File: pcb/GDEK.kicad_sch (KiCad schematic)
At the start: 266 parts, among them J1 TYPE-C-31-M-13C, J101 TYPE-C-31-M-13C, J102 AudioJack4, J103 Debug pads, J2 AudioJack4, J3 Debug pads, SW1 SK6812MINI, SW10 SK6812MINI, SW101 SK6812MINI, SW102 SK6812MINI, SW103 SK6812MINI, SW104 SK6812MINI, SW105 SK6812MINI, SW106 SK6812MINI, SW107 SK6812MINI, SW108 SK6812MINI, SW109 SK6812MINI, SW11 SK6812MINI, SW110 SK6812MINI, SW111 SK6812MINI, SW112 SK6812MINI, SW113 SK6812MINI, SW114 SK6812MINI, SW115 SK6812MINI, SW116 SK6812MINI, SW117 SK6812MINI, SW118 SK6812MINI, SW119 SK6812MINI, SW12 SK6812MINI, SW120 SK6812MINI, SW121 SK6812MINI, SW122 SK6812MINI, SW123 SK6812MINI, SW124 SK6812MINI, SW125 SK6812MINI, SW126 SK6812MINI, SW127 SK6812MINI, SW128 SK6812MINI, SW129 SK6812MINI, SW13 SK6812MINI, SW130 SK6812MINI, SW131 RotaryEncoder_Switch, SW14 SK6812MINI, SW15 SK6812MINI, SW16 SK6812MINI, SW17 SK6812MINI, SW18 SK6812MINI, SW19 SK6812MINI, SW2 SK6812MINI, SW20 SK6812MINI, SW21 SK6812MINI, SW22 SK6812MINI, SW23 SK6812MINI, SW24 SK6812MINI, SW25 SK6812MINI, SW26 SK6812MINI, SW27 SK6812MINI, SW28 SK6812MINI, SW29 SK6812MINI, SW3 SK6812MINI, SW30 SK6812MINI, SW31 RotaryEncoder_Switch, SW4 SK6812MINI, SW5 SK6812MINI, SW6 SK6812MINI, SW7 SK6812MINI, SW8 SK6812MINI, SW9 SK6812MINI, U1 RP2040, U101 RP2040, U102 W25Q128JVS, U103 74AHCT1G125, U104 USBLC6-2P6, U105 XC6210B332MR, U2 W25Q128JVS, U3 74AHCT1G125, U4 USBLC6-2P6, U5 XC6210B332MR, Y1 ABM8-272-T3, Y101 ABM8-272-T3

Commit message: ♻️ Replace LED and reroute them
They are flipped on odd rows to have a better layout not requiring any layer switch because of the new LED footprint with mouse ears.
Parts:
- removed SW1, SW10, SW101, SW102, SW103, SW104, SW105, SW106, SW107, SW108, SW109, SW11, SW110, SW111, SW112, SW113, SW114, SW115, SW116, SW117, SW118, SW119, SW12, SW120, SW121, SW122, SW123, SW124, SW125, SW126, SW127, SW128, SW129, SW13, SW130, SW14, SW15, SW16, SW17, SW18, SW19, SW2, SW20, SW21, SW22, SW23, SW24, SW25, SW26, SW27, SW28, SW29, SW3, SW30, SW4, SW5, SW6, SW7, SW8, SW9: SK6812MINI, GDEK:MX+KailhChoc+GateronKS+SK6812MINI-E_Tight, symbol GDEK:SW+SK6812MINIE
- added LD1, LD10, LD101, LD102, LD103, LD104, LD105, LD106, LD107, LD108, LD109, LD11, LD110, LD111, LD112, LD113, LD114, LD115, LD116, LD117, LD118, LD119, LD12, LD120, LD121, LD122, LD123, LD124, LD125, LD126, LD127, LD128, LD129, LD13, LD130, LD14, LD15, LD16, LD17, LD18, LD19, LD2, LD20, LD21, LD22, LD23, LD24, LD25, LD26, LD27, LD28, LD29, LD3, LD30, LD4, LD5, LD6, LD7, LD8, LD9: SK6812, GDEK:SK6812MINIE, symbol LED:SK6812
- added SW1, SW10, SW101, SW102, SW103, SW104, SW105, SW106, SW107, SW108, SW109, SW11, SW110, SW111, SW112, SW113, SW114, SW115, SW116, SW117, SW118, SW119, SW12, SW120, SW121, SW122, SW123, SW124, SW125, SW126, SW127, SW128, SW129, SW13, SW130, SW14, SW15, SW16, SW17, SW18, SW19, SW2, SW20, SW21, SW22, SW23, SW24, SW25, SW26, SW27, SW28, SW29, SW3, SW30, SW4, SW5, SW6, SW7, SW8, SW9: SW_Push_45deg, GDEK:MX+KailhChoc+GateronKS_Tight, symbol Switch:SW_Push_45deg
- U102, U2: footprint Package_SO:SOIC-8_5.23x5.23mm_P1.27mm -> Package_SO:SOIC-8_5.3x5.3mm_P1.27mm
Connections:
- net +5V: now also LD1.3 (VDD), LD10.3 (VDD), LD11.3 (VDD), LD12.3 (VDD), LD13.3 (VDD), LD14.3 (VDD), LD15.3 (VDD), LD16.3 (VDD), LD17.3 (VDD), LD18.3 (VDD), LD19.3 (VDD), LD2.3 (VDD), LD20.3 (VDD), LD21.3 (VDD), LD22.3 (VDD), LD23.3 (VDD), LD24.3 (VDD), LD25.3 (VDD), LD26.3 (VDD), LD27.3 (VDD), LD28.3 (VDD), LD29.3 (VDD), LD3.3 (VDD), LD30.3 (VDD), LD4.3 (VDD), LD5.3 (VDD), LD6.3 (VDD), LD7.3 (VDD), LD8.3 (VDD), LD9.3 (VDD)
- net +5V_R: now also LD101.3 (VDD), LD102.3 (VDD), LD103.3 (VDD), LD104.3 (VDD), LD105.3 (VDD), LD106.3 (VDD), LD107.3 (VDD), LD108.3 (VDD), LD109.3 (VDD), LD110.3 (VDD), LD111.3 (VDD), LD112.3 (VDD), LD113.3 (VDD), LD114.3 (VDD), LD115.3 (VDD), LD116.3 (VDD), LD117.3 (VDD), LD118.3 (VDD), LD119.3 (VDD), LD120.3 (VDD), LD121.3 (VDD), LD122.3 (VDD), LD123.3 (VDD), LD124.3 (VDD), LD125.3 (VDD), LD126.3 (VDD), LD127.3 (VDD), LD128.3 (VDD), LD129.3 (VDD), LD130.3 (VDD)
- net COL0: now also SW1.1, SW13.1, SW19.1, SW25.1, SW7.1
- net COL0_R: now also SW101.1, SW107.1, SW113.1, SW119.1, SW125.1
- net COL1: now also SW14.1, SW2.1, SW20.1, SW26.1, SW8.1
- net COL1_R: now also SW102.1, SW108.1, SW114.1, SW120.1, SW126.1
- net COL2: now also SW15.1, SW21.1, SW27.1, SW3.1, SW9.1
- net COL2_R: now also SW103.1, SW109.1, SW115.1, SW121.1, SW127.1
- net COL3: now also SW10.1, SW16.1, SW22.1, SW28.1, SW4.1
- net COL3_R: now also SW104.1, SW110.1, SW116.1, SW122.1, SW128.1
- net COL4: now also SW11.1, SW17.1, SW23.1, SW29.1, SW5.1
- net COL4_R: now also SW105.1, SW111.1, SW117.1, SW123.1, SW129.1
- net COL5: now also SW12.1, SW18.1, SW24.1, SW30.1, SW6.1
- net COL5_R: now also SW106.1, SW112.1, SW118.1, SW124.1, SW130.1
- net GND: now also LD1.1 (VSS), LD10.1 (VSS), LD11.1 (VSS), LD12.1 (VSS), LD13.1 (VSS), LD14.1 (VSS), LD15.1 (VSS), LD16.1 (VSS), LD17.1 (VSS), LD18.1 (VSS), LD19.1 (VSS), LD2.1 (VSS), LD20.1 (VSS), LD21.1 (VSS), LD22.1 (VSS), LD23.1 (VSS), LD24.1 (VSS), LD25.1 (VSS), LD26.1 (VSS), LD27.1 (VSS), LD28.1 (VSS), LD29.1 (VSS), LD3.1 (VSS), LD30.1 (VSS), LD4.1 (VSS), LD5.1 (VSS), LD6.1 (VSS), LD7.1 (VSS), LD8.1 (VSS), LD9.1 (VSS)
- net GND_R: now also LD101.1 (VSS), LD102.1 (VSS), LD103.1 (VSS), LD104.1 (VSS), LD105.1 (VSS), LD106.1 (VSS), LD107.1 (VSS), LD108.1 (VSS), LD109.1 (VSS), LD110.1 (VSS), LD111.1 (VSS), LD112.1 (VSS), LD113.1 (VSS), LD114.1 (VSS), LD115.1 (VSS), LD116.1 (VSS), LD117.1 (VSS), LD118.1 (VSS), LD119.1 (VSS), LD120.1 (VSS), LD121.1 (VSS), LD122.1 (VSS), LD123.1 (VSS), LD124.1 (VSS), LD125.1 (VSS), LD126.1 (VSS), LD127.1 (VSS), LD128.1 (VSS), LD129.1 (VSS), LD130.1 (VSS)
- net at D30.2 (A): now also SW30.2
- net at D120.2 (A): now also SW120.2
- net at D17.2 (A): now also SW17.2
- net at D110.2 (A): now also SW110.2
- net at D121.2 (A): now also SW121.2
- net at D29.2 (A): now also SW29.2
- net at D10.2 (A): now also SW10.2
- net at D128.2 (A): now also SW128.2
- net at D16.2 (A): now also SW16.2
- net at D126.2 (A): now also SW126.2
- net at U103.4: now also LD106.2 (DIN)
- net at D14.2 (A): now also SW14.2
- net at D23.2 (A): now also SW23.2
- net at D9.2 (A): now also SW9.2
- net at D25.2 (A): now also SW25.2
- net at D115.2 (A): now also SW115.2
- net at D4.2 (A): now also SW4.2
- net at D124.2 (A): now also SW124.2
- net at D20.2 (A): now also SW20.2
- net at D7.2 (A): now also SW7.2
- net at D22.2 (A): now also SW22.2
- net at D18.2 (A): now also SW18.2
- net at D101.2 (A): now also SW101.2
- net at D15.2 (A): now also SW15.2
- net at D2.2 (A): now also SW2.2
- net at D109.2 (A): now also SW109.2
- net at D127.2 (A): now also SW127.2
- net at D13.2 (A): now also SW13.2
- net at D26.2 (A): now also SW26.2
- net at D21.2 (A): now also SW21.2
- net at D106.2 (A): now also SW106.2
- net at D122.2 (A): now also SW122.2
- net at D3.2 (A): now also SW3.2
- net at D117.2 (A): now also SW117.2
- net at D130.2 (A): now also SW130.2
- net at D107.2 (A): now also SW107.2
- net at D119.2 (A): now also SW119.2
- net at D28.2 (A): now also SW28.2
- net at D8.2 (A): now also SW8.2
- net at D11.2 (A): now also SW11.2
- net at D5.2 (A): now also SW5.2
- net at D102.2 (A): now also SW102.2
- net at D24.2 (A): now also SW24.2
- net at D118.2 (A): now also SW118.2
- net at D104.2 (A): now also SW104.2
- net at D129.2 (A): now also SW129.2
- net at D12.2 (A): now also SW12.2
- net at D6.2 (A): now also SW6.2
- net at D108.2 (A): now also SW108.2
- net at D27.2 (A): now also SW27.2
- net at D103.2 (A): now also SW103.2
- net at D123.2 (A): now also SW123.2
- net at D1.2 (A): now also SW1.2
- net at U3.4: now also LD6.2 (DIN)
- net at D113.2 (A): now also SW113.2
- net at D114.2 (A): now also SW114.2
- net at D19.2 (A): now also SW19.2
- net at D105.2 (A): now also SW105.2
- net at D125.2 (A): now also SW125.2
- net at D111.2 (A): now also SW111.2
- net at D116.2 (A): now also SW116.2
- net at D112.2 (A): now also SW112.2
- new net: LD129.2 (DIN), LD130.4 (DOUT)
- new net: LD128.2 (DIN), LD129.4 (DOUT)
- new net: LD107.4 (DOUT), LD108.2 (DIN)
- new net: LD108.4 (DOUT), LD109.2 (DIN)
- new net: LD122.4 (DOUT), LD123.2 (DIN)
- new net: LD123.4 (DOUT), LD124.2 (DIN)
- new net: LD7.4 (DOUT), LD8.2 (DIN)
- new net: LD8.4 (DOUT), LD9.2 (DIN)
- new net: LD114.2 (DIN), LD115.4 (DOUT)
- new net: LD113.2 (DIN), LD114.4 (DOUT)
- new net: LD14.2 (DIN), LD15.4 (DOUT)
- new net: LD13.2 (DIN), LD14.4 (DOUT)
- new net: LD113.4 (DOUT), LD119.2 (DIN)
- new net: LD23.4 (DOUT), LD24.2 (DIN)
- new net: LD24.4 (DOUT), LD30.2 (DIN)
- new net: LD27.2 (DIN), LD28.4 (DOUT)
- new net: LD26.2 (DIN), LD27.4 (DOUT)
- new net: LD101.2 (DIN), LD102.4 (DOUT)
- new net: LD101.4 (DOUT), LD107.2 (DIN)
- new net: LD121.4 (DOUT), LD122.2 (DIN)
- new net: LD28.2 (DIN), LD29.4 (DOUT)
- new net: LD5.2 (DIN), LD6.4 (DOUT)
- new net: LD4.2 (DIN), LD5.4 (DOUT)
- new net: LD127.2 (DIN), LD128.4 (DOUT)
- new net: LD126.2 (DIN), LD127.4 (DOUT)
- new net: LD109.4 (DOUT), LD110.2 (DIN)
- new net: LD2.2 (DIN), LD3.4 (DOUT)
- new net: LD1.2 (DIN), LD2.4 (DOUT)
- new net: LD104.2 (DIN), LD105.4 (DOUT)
- new net: LD103.2 (DIN), LD104.4 (DOUT)
- new net: LD13.4 (DOUT), LD19.2 (DIN)
- new net: LD16.2 (DIN), LD17.4 (DOUT)
- new net: LD15.2 (DIN), LD16.4 (DOUT)
- new net: LD116.2 (DIN), LD117.4 (DOUT)
- new net: LD115.2 (DIN), LD116.4 (DOUT)
- new net: LD3.2 (DIN), LD4.4 (DOUT)
- new net: LD25.2 (DIN), LD26.4 (DOUT)
- new net: LD19.4 (DOUT), LD20.2 (DIN)
- new net: LD20.4 (DOUT), LD21.2 (DIN)
- new net: LD125.2 (DIN), LD126.4 (DOUT)
- new net: LD120.4 (DOUT), LD121.2 (DIN)
- new net: LD119.4 (DOUT), LD120.2 (DIN)
- new net: LD11.4 (DOUT), LD12.2 (DIN)
- new net: LD12.4 (DOUT), LD18.2 (DIN)
- new net: LD124.4 (DOUT), LD130.2 (DIN)
- new net: LD10.2 (DIN), LD9.4 (DOUT)
- new net: LD105.2 (DIN), LD106.4 (DOUT)
- new net: LD21.4 (DOUT), LD22.2 (DIN)
- new net: LD29.2 (DIN), LD30.4 (DOUT)
- new net: LD102.2 (DIN), LD103.4 (DOUT)
- new net: LD17.2 (DIN), LD18.4 (DOUT)
- new net: LD22.4 (DOUT), LD23.2 (DIN)
- new net: LD117.2 (DIN), LD118.4 (DOUT)
- new net: LD10.4 (DOUT), LD11.2 (DIN)
- new net: LD1.4 (DOUT), LD7.2 (DIN)
- new net: LD111.4 (DOUT), LD112.2 (DIN)
- new net: LD112.4 (DOUT), LD118.2 (DIN)
- new net: LD110.4 (DOUT), LD111.2 (DIN)
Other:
- moved on the sheet: U102, U2

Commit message: ✨ Update lots of stuff (and make the thumb cluster round)
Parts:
- LD1, LD10, LD101, LD102, LD103, LD104, LD105, LD106, LD107, LD108, LD109, LD11, LD110, LD111, LD112, LD113, LD114, LD115, LD116, LD117, LD118, LD119, LD12, LD120, LD121, LD122, LD123, LD124, LD125, LD126, LD127, LD128, LD129, LD13, LD130, LD14, LD15, LD16, LD17, LD18, LD19, LD2, LD20, LD21, LD22, LD23, LD24, LD25, LD26, LD27, LD28, LD29, LD3, LD30, LD4, LD5, LD6, LD7, LD8, LD9: LCSC (none) -> C5149201
- R1, R10, R101, R110: value 1kΩ -> 1k
- R102, R2: value 5.1kΩ -> 5.1k
- R105, R11, R111, R5: value 470Ω -> 470
- R106, R107, R6, R7: value 27Ω -> 27

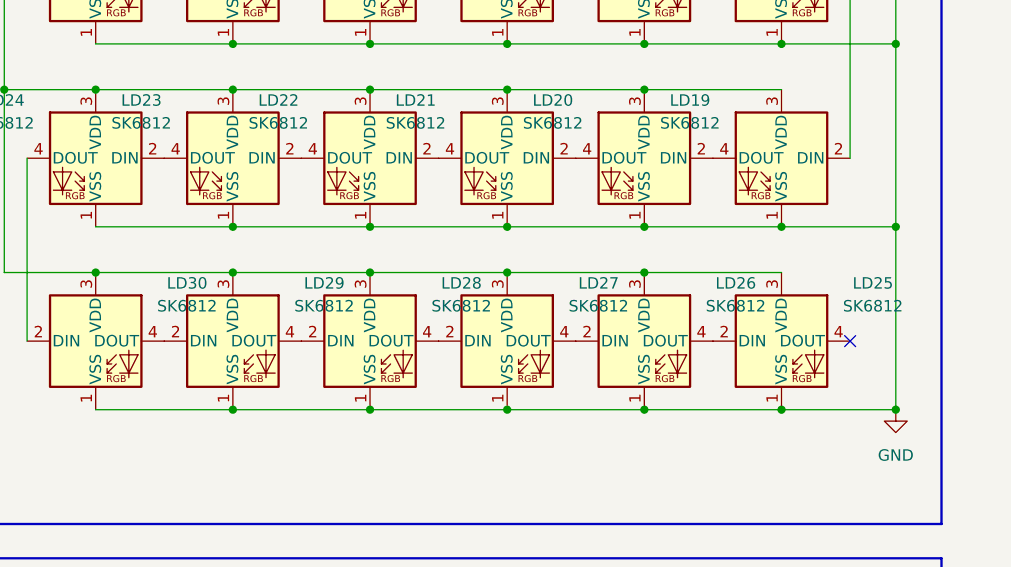
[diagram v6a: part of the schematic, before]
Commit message: ✨ Route LED power and decoupling
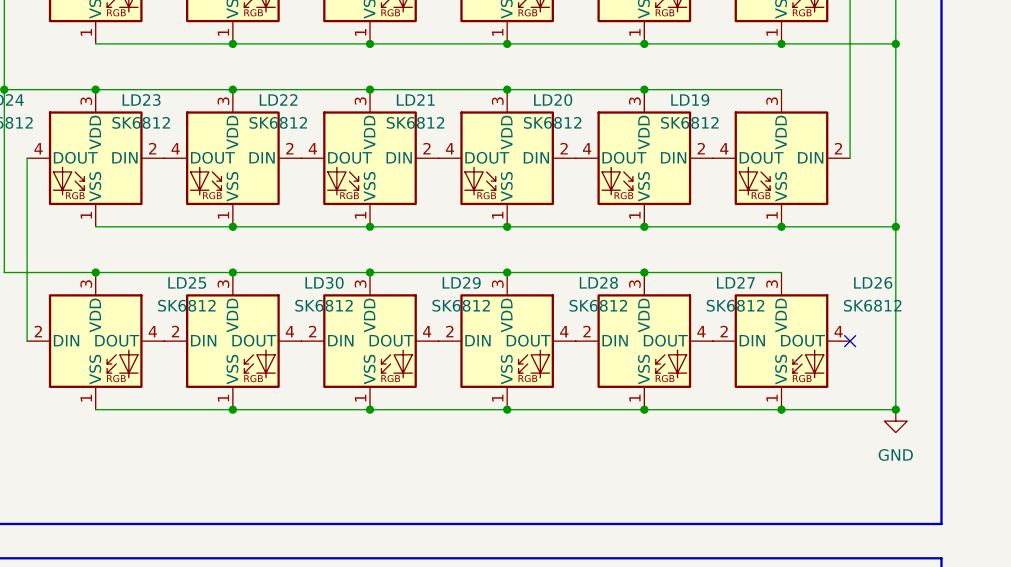
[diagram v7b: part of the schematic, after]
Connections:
- net at LD24.4 (DOUT): now also LD25.2 (DIN); no longer LD30.2 (DIN)
- net at LD26.4 (DOUT): no longer LD25.2 (DIN)
- net at LD25.4 (DOUT): now also LD30.2 (DIN)
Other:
- moved on the sheet: LD25, LD26, LD27, LD28, LD29, LD30
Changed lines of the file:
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@@
 	)
 	(junction
-		(at 386.08 134.62)
-		(diameter 0)
-		(color 0 0 0 0)
-	)
-	(junction
 		(at 332.74 420.37)
 		(diameter 0)
@@
 	)
 	(junction
+		(at 386.08 134.62)
+		(diameter 0)
+		(color 0 0 0 0)
+	)
+	(junction
 		(at 233.68 86.36)
 		(diameter 0)
@@
 	)
 	(junction
-		(at 309.88 119.38)
-		(diameter 0)
-		(color 0 0 0 0)
-	)
-	(junction
 		(at 325.12 93.98)
 		(diameter 0)
@@
 	)
 	(junction
+		(at 309.88 119.38)
+		(diameter 0)
+		(color 0 0 0 0)
+	)
+	(junction
 		(at 137.16 276.86)
 		(diameter 0)
@@
 	(wire
 		(pts
+			(xy 386.08 134.62) (xy 398.78 134.62)
+		)
+		(stroke
+			(width 0)
+			(type default)
+		)
+	)
+	(wire
+		(pts
 			(xy 307.34 194.31) (xy 307.34 207.01)
 		)
@@
 	(wire
 		(pts
-			(xy 386.08 134.62) (xy 398.78 134.62)
-		)
-		(stroke
-			(width 0)
-			(type default)
-		)
-	)
-	(wire
-		(pts
 			(xy 304.8 227.33) (xy 317.5 227.33)
 		)
@@
 	(wire
 		(pts
+			(xy 309.88 119.38) (xy 325.12 119.38)
+		)
+		(stroke
+			(width 0)
+			(type default)
+		)
+	)
+	(wire
+		(pts
 			(xy 304.8 189.23) (xy 317.5 189.23)
 		)
@@
 	(wire
 		(pts
-			(xy 309.88 119.38) (xy 325.12 119.38)
-		)
-		(stroke
-			(width 0)
-			(type default)
-		)
-	)
-	(wire
-		(pts
 			(xy 121.92 344.17) (xy 135.89 344.17)
 		)
@@
 	(symbol
 		(lib_id "LED:SK6812")
-		(at 355.6 127 0)
+		(at 370.84 127 0)
 		(unit 1)
 		(exclude_from_sim no)
@@
 		(fields_autoplaced yes)
 		(property "Reference" "LD27"
-			(at 365.76 120.5798 0)
+			(at 381 120.5798 0)
 			(effects
 				(font
@@
 		)
 		(property "Value" "SK6812"
-			(at 365.76 123.1198 0)
+			(at 381 123.1198 0)
 			(effects
 				(font
@@
 		)
 		(property "Footprint" "GDEK:SK6812MINIE"
-			(at 356.87 134.62 0)
+			(at 372.11 134.62 0)
 			(effects
 				(font
@@
 		)
 		(property "Datasheet" "https://cdn-shop.adafruit.com/product-files/1138/SK6812+LED+datasheet+.pdf"
-			(at 358.14 136.525 0)
+			(at 373.38 136.525 0)
 			(effects
 				(font
@@
 		)
 		(property "Description" "RGB LED with integrated controller"
-			(at 355.6 127 0)
+			(at 370.84 127 0)
 			(effects
 				(font
@@
 		)
 		(property "LCSC" "C5149201"
-			(at 355.6 127 0)
+			(at 370.84 127 0)
 			(effects
 				(font
@@
 	(symbol
 		(lib_id "LED:SK6812")
-		(at 340.36 127 0)
+		(at 355.6 127 0)
 		(unit 1)
 		(exclude_from_sim no)
@@
 		(fields_autoplaced yes)
 		(property "Reference" "LD28"
-			(at 350.52 120.5798 0)
+			(at 365.76 120.5798 0)
 			(effects
 				(font
@@
 		)
 		(property "Value" "SK6812"
-			(at 350.52 123.1198 0)
+			(at 365.76 123.1198 0)
 			(effects
 				(font
@@
 		)
 		(property "Footprint" "GDEK:SK6812MINIE"
-			(at 341.63 134.62 0)
+			(at 356.87 134.62 0)
 			(effects
 				(font
@@
 		)
 		(property "Datasheet" "https://cdn-shop.adafruit.com/product-files/1138/SK6812+LED+datasheet+.pdf"
-			(at 342.9 136.525 0)
+			(at 358.14 136.525 0)
 			(effects
 				(font
@@
 		)
 		(property "Description" "RGB LED with integrated controller"
-			(at 340.36 127 0)
+			(at 355.6 127 0)
 			(effects
 				(font
@@
 		)
 		(property "LCSC" "C5149201"
-			(at 340.36 127 0)
+			(at 355.6 127 0)
 			(effects
 				(font
@@
 	(symbol
 		(lib_id "LED:SK6812")
-		(at 370.84 127 0)
+		(at 386.08 127 0)
 		(unit 1)
 		(exclude_from_sim no)
@@
 		(fields_autoplaced yes)
 		(property "Reference" "LD26"
-			(at 381 120.5798 0)
+			(at 396.24 120.5798 0)
 			(effects
 				(font
@@
 		)
 		(property "Value" "SK6812"
-			(at 381 123.1198 0)
+			(at 396.24 123.1198 0)
 			(effects
 				(font
@@
 		)
 		(property "Footprint" "GDEK:SK6812MINIE"
-			(at 372.11 134.62 0)
+			(at 387.35 134.62 0)
 			(effects
 				(font
@@
 		)
 		(property "Datasheet" "https://cdn-shop.adafruit.com/product-files/1138/SK6812+LED+datasheet+.pdf"
-			(at 373.38 136.525 0)
+			(at 388.62 136.525 0)
 			(effects
 				(font
@@
 		)
 		(property "Description" "RGB LED with integrated controller"
-			(at 370.84 127 0)
+			(at 386.08 127 0)
 			(effects
 				(font
@@
 		)
 		(property "LCSC" "C5149201"
-			(at 370.84 127 0)
+			(at 386.08 127 0)
 			(effects
 				(font
@@
 	(symbol
 		(lib_id "LED:SK6812")
-		(at 386.08 127 0)
+		(at 309.88 127 0)
 		(unit 1)
 		(exclude_from_sim no)
@@
 		(fields_autoplaced yes)
 		(property "Reference" "LD25"
-			(at 396.24 120.5798 0)
+			(at 320.04 120.5798 0)
 			(effects
 				(font
@@
 		)
 		(property "Value" "SK6812"
-			(at 396.24 123.1198 0)
+			(at 320.04 123.1198 0)
 			(effects
 				(font
@@
 		)
 		(property "Footprint" "GDEK:SK6812MINIE"
-			(at 387.35 134.62 0)
+			(at 311.15 134.62 0)
 			(effects
 				(font
@@
 		)
 		(property "Datasheet" "https://cdn-shop.adafruit.com/product-files/1138/SK6812+LED+datasheet+.pdf"
-			(at 388.62 136.525 0)
+			(at 312.42 136.525 0)
 			(effects
 				(font
@@
 		)
 		(property "Description" "RGB LED with integrated controller"
-			(at 386.08 127 0)
+			(at 309.88 127 0)
 			(effects
 				(font
@@
 		)
 		(property "LCSC" "C5149201"
-			(at 386.08 127 0)
+			(at 309.88 127 0)
 			(effects
 				(font
@@
 	(symbol
 		(lib_id "LED:SK6812")
-		(at 309.88 127 0)
+		(at 325.12 127 0)
 		(unit 1)
 		(exclude_from_sim no)
@@
 		(fields_autoplaced yes)
 		(property "Reference" "LD30"
-			(at 320.04 120.5798 0)
+			(at 335.28 120.5798 0)
 			(effects
 				(font
@@
 		)
 		(property "Value" "SK6812"
-			(at 320.04 123.1198 0)
+			(at 335.28 123.1198 0)
 			(effects
 				(font
@@
 		)
 		(property "Footprint" "GDEK:SK6812MINIE"
-			(at 311.15 134.62 0)
+			(at 326.39 134.62 0)
 			(effects
 				(font
@@
 		)
 		(property "Datasheet" "https://cdn-shop.adafruit.com/product-files/1138/SK6812+LED+datasheet+.pdf"
-			(at 312.42 136.525 0)
+			(at 327.66 136.525 0)
 			(effects
 				(font
@@
 		)
 		(property "Description" "RGB LED with integrated controller"
-			(at 309.88 127 0)
+			(at 325.12 127 0)
 			(effects
 				(font
@@
 		)
 		(property "LCSC" "C5149201"
-			(at 309.88 127 0)
+			(at 325.12 127 0)
 			(effects
 				(font
@@
 	(symbol
 		(lib_id "LED:SK6812")
-		(at 325.12 127 0)
+		(at 340.36 127 0)
 		(unit 1)
 		(exclude_from_sim no)
@@
 		(fields_autoplaced yes)
 		(property "Reference" "LD29"
-			(at 335.28 120.5798 0)
+			(at 350.52 120.5798 0)
 			(effects
 				(font
@@
 		)
 		(property "Value" "SK6812"
-			(at 335.28 123.1198 0)
+			(at 350.52 123.1198 0)
 			(effects
 				(font
@@
 		)
 		(property "Footprint" "GDEK:SK6812MINIE"
-			(at 326.39 134.62 0)
+			(at 341.63 134.62 0)
 			(effects
 				(font
@@
 		)
 		(property "Datasheet" "https://cdn-shop.adafruit.com/product-files/1138/SK6812+LED+datasheet+.pdf"
-			(at 327.66 136.525 0)
+			(at 342.9 136.525 0)
 			(effects
 				(font
@@
 		)
 		(property "Description" "RGB LED with integrated controller"
-			(at 325.12 127 0)
+			(at 340.36 127 0)
 			(effects
 				(font
@@
 		)
 		(property "LCSC" "C5149201"
-			(at 325.12 127 0)
+			(at 340.36 127 0)
 			(effects
 				(font

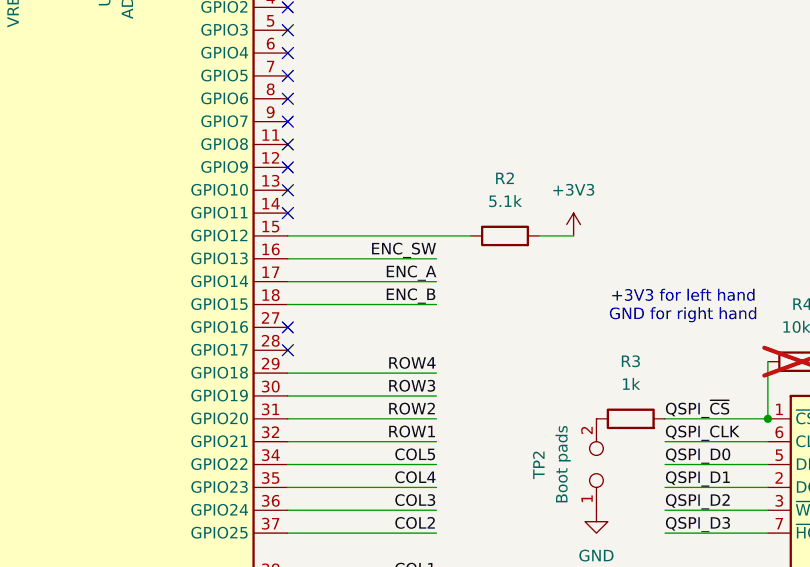
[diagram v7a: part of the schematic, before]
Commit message: ✨ Route LED power rails
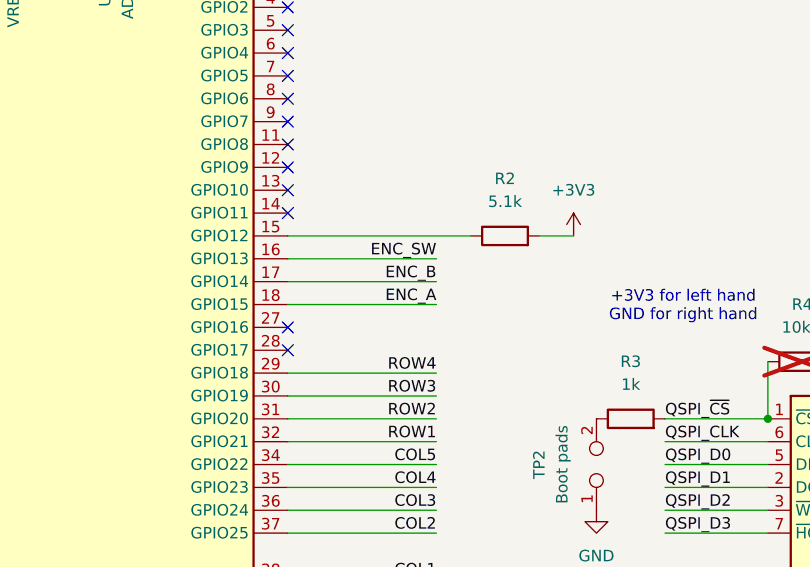
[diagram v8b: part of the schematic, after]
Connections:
- net ENC_A: now also U1.18 (GPIO15); no longer U1.17 (GPIO14)
- net ENC_B: now also U1.17 (GPIO14); no longer U1.18 (GPIO15)
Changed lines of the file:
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@@
 	)
 	(label "ENC_B"
-		(at 128.27 175.26 180)
+		(at 128.27 172.72 180)
 		(effects
 			(font
@@
 	)
 	(label "ENC_A"
-		(at 128.27 172.72 180)
-		(effects
-			(font
+		(at 128.27 175.26 180)
+		(effects
+			(font
